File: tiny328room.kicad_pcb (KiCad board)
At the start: 2 copper layers, 105.7 x 23.5 mm, 12 parts, among them K1 PIR, U1 DS18B20, U2 DHT11, U3 TINY328

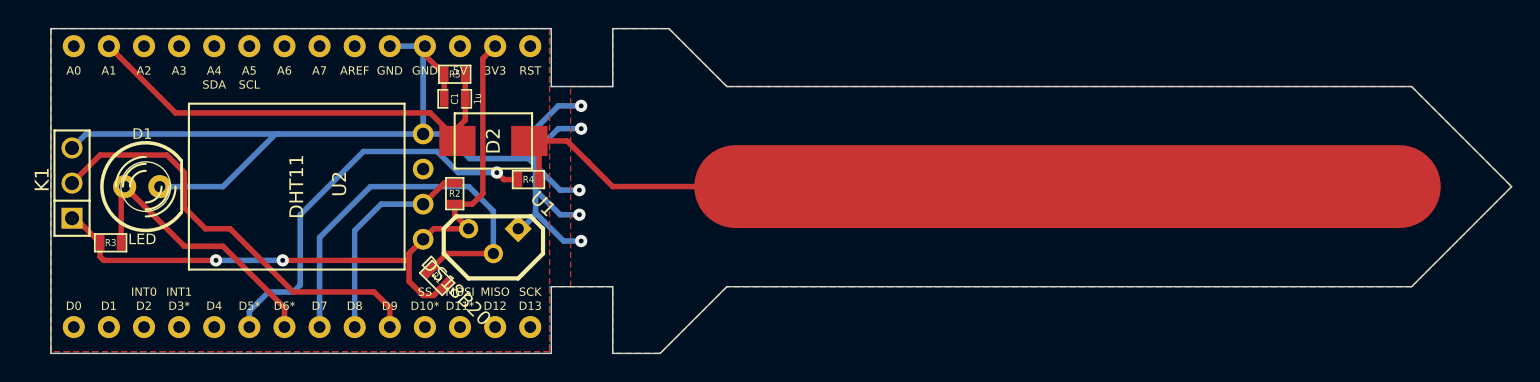
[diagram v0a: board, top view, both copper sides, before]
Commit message: add ambient light sensor
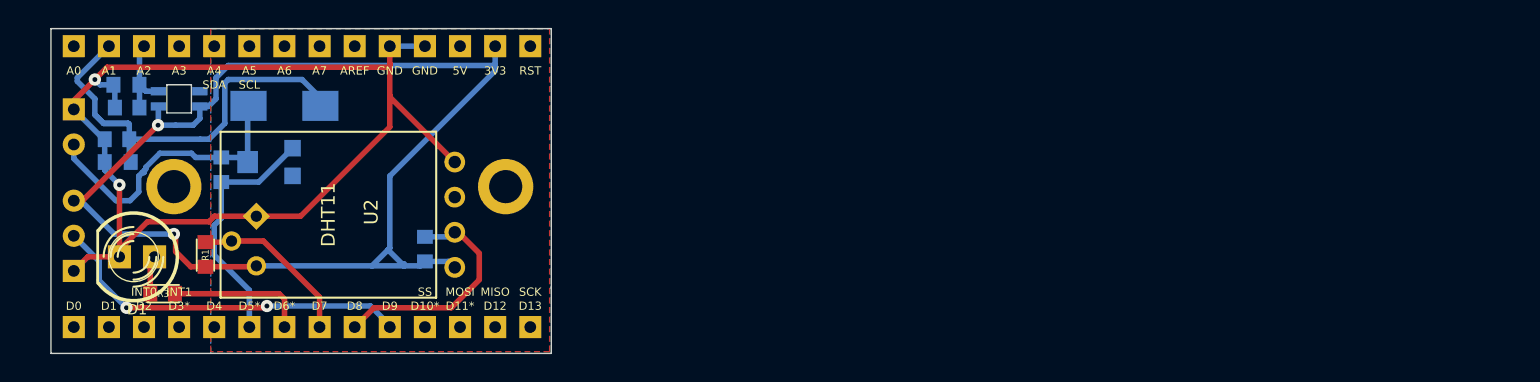
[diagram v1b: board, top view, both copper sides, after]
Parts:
- added 1PIN: P***, 1pin_only, F.Cu at (74.8, 69.8)
- added 1PIN: P***, 1pin_only, F.Cu at (50.8, 69.8)
- added C2: 0.1u, SM0603_C_Hand, B.Cu at (47.4, 62.5)
- added K2: SOIL, PIN_ARRAY_2X1, B.Cu at (43.6, 65.5)
- added R6: 5k, SM0603_Hand, B.Cu at (47.4, 64.1)
- added RV1: 20k, 3305_POT, B.Cu at (57.8, 68.1)
- added U4: APDS-9006-020, APDS-9006-020, B.Cu at (51.2, 63.5)
- C1: footprint SM0603_Capa -> SM0603_C_Hand; moved to B.Cu
- D2, K1, U1: moved to B.Cu
- R1, R3: footprint SM0603 -> SM0603_Hand
- R2, R4, R5: footprint SM0603 -> SM0603_Hand; moved to B.Cu
- moved R5 24.8 mm to (46.7, 66.4)
- moved C1 24.8 mm to (46.7, 68.1)
- moved R4 22.2 mm to (54.2, 68.6), turned to 270 degrees
- moved U1 17.2 mm to (56.8, 73.8), turned to 315 degrees
- moved R1 16.8 mm to (53.1, 74.8), turned to 90 degrees
- moved D2 15.3 mm to (58.8, 64.0), turned to 0 degrees
- moved R3 5.30 mm to (50.0, 77.6), turned to 180 degrees
- moved D1 5.09 mm to (48.1, 74.9), turned to 180 degrees
- moved R2 4.60 mm to (69.0, 74.4)
- moved K1 3.81 mm to (43.6, 73.4), turned to 270 degrees
- moved U2 3.06 mm to (62.0, 71.9)
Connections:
- D1 pad 1: /LED -> N-000004
- R3 pad 1: 3V3 -> /LED
- R3 pad 2: /LED -> N-000004
- U3 pad 17: (no net) -> /BRIGHT
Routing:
- net /CAP_SENSE: track 67.4 -> 21.4 mm
- net 3V3: track 52.2 -> 89.4 mm
- net /DS: track 29.5 -> 12.1 mm
- net N-0000010: track 29.2 -> 17.9 mm, vias 1 -> 0
- net /LED: track 20.8 -> 10.1 mm
- net /BRIGHT: track 0.00 -> 6.14 mm
- net /PIR: track 31.3 -> 26.6 mm, vias 0 -> 2
- net GND: track 86.3 -> 82.8 mm, vias 5 -> 2
- net N-000004: track 0.00 -> 2.79 mm
- net /DHT: track 15.6 -> 17.0 mm
- removed copper zone on F.Cu, net GND
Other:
- board size 105.7 x 23.5 mm -> 36.2 x 23.5 mm
- board text added: "GND"
- board text added: "PIR"
- board text added: "SOIL"
- board text added: "VCC"

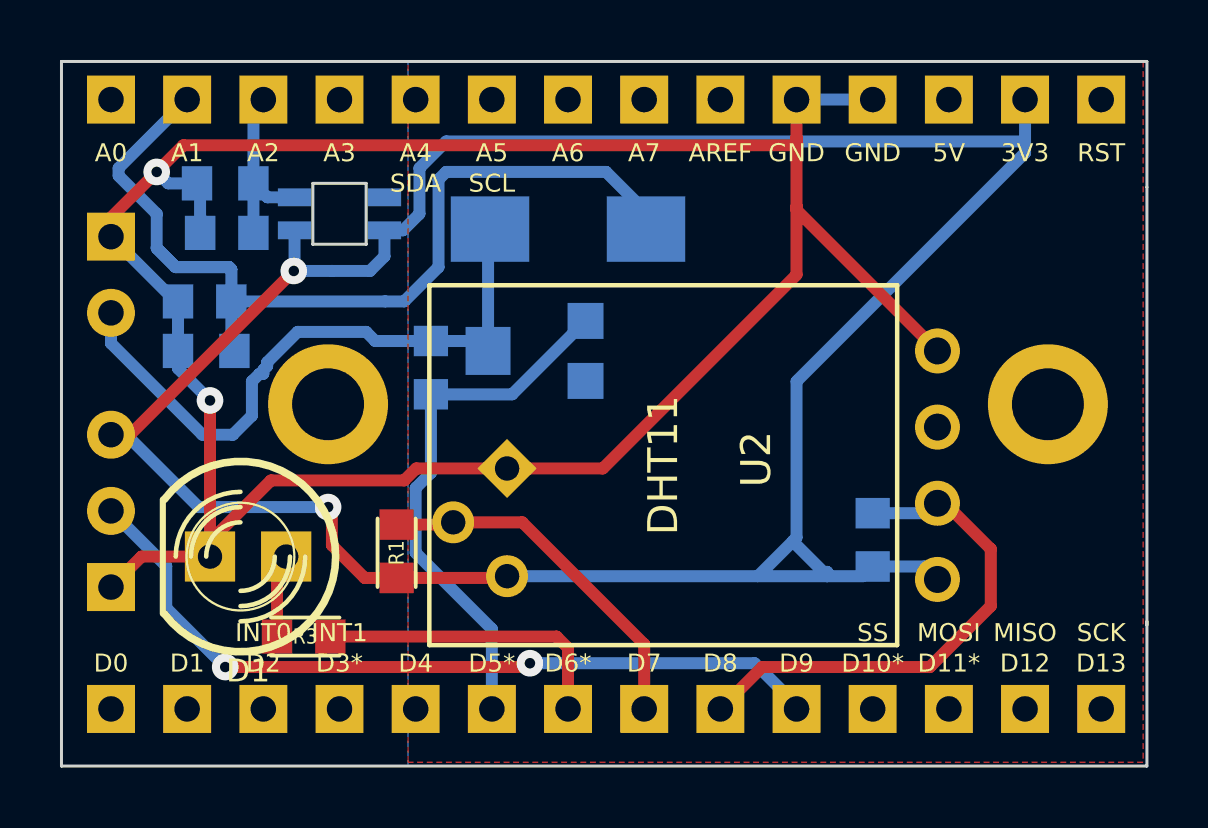
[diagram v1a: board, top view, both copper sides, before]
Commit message: added ultrasonic distance measurer
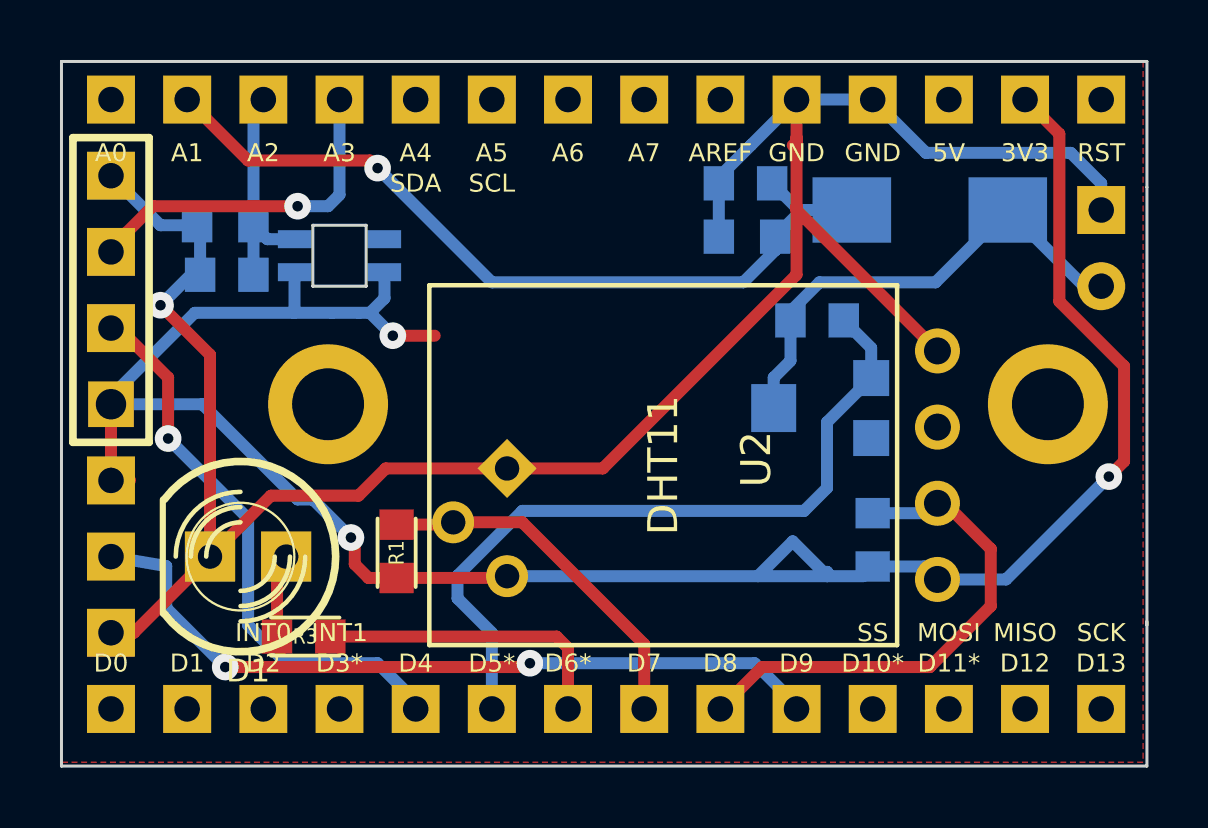
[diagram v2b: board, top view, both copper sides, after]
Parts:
- added K3: DIST, PIN_ARRAY_4x1, F.Cu at (43.6, 66.0)
- moved K2 33.0 mm to (76.6, 64.6)
- moved R5 18.5 mm to (64.8, 62.5)
- moved C1 18.4 mm to (64.8, 64.3)
- moved R4 12.9 mm to (67.1, 67.1), turned to 0 degrees
- moved D2 12.1 mm to (70.9, 63.4), turned to 180 degrees
- moved RV1 9.71 mm to (67.3, 70.0)
- moved K1 1.52 mm to (43.6, 74.9)
- moved U4 1.40 mm to (51.2, 64.9)
- moved C2 1.40 mm to (47.4, 63.9)
- moved R6 1.40 mm to (47.4, 65.5)
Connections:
- net N-0000010 renamed /CAP_TRIG
- net N-000002 renamed /CAP_OUT
- U3 pad 18: (no net) -> /DIST_ECHO
- U3 pad 5: (no net) -> /DIST_TRIG
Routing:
- net /DIST_TRIG: track 0.00 -> 18.8 mm, vias 0 -> 1
- net 3V3: track 89.4 -> 74.2 mm, vias 2 -> 3
- net /DIST_ECHO: track 0.00 -> 11.7 mm, vias 0 -> 1
- net GND: track 82.8 -> 74.9 mm, vias 2 -> 1
- net /CAP_TRIG: track 17.9 -> 25.0 mm
- net /CAP_SENSE: track 21.4 -> 16.7 mm
- net /CAP_OUT: track 33.2 -> 29.0 mm, vias 0 -> 1
- net /BRIGHT: track 6.14 -> 8.01 mm
- net /PIR: track 26.6 -> 25.9 mm
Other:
- outline, holes or cut-outs redrawn
- board text added: "3V3"
- board text added: "CAP SENSE"
- board text added: "DIST_TRIG"
- board text added: "ECHO"
- board text removed: "SOIL"
- board text removed: "VCC"

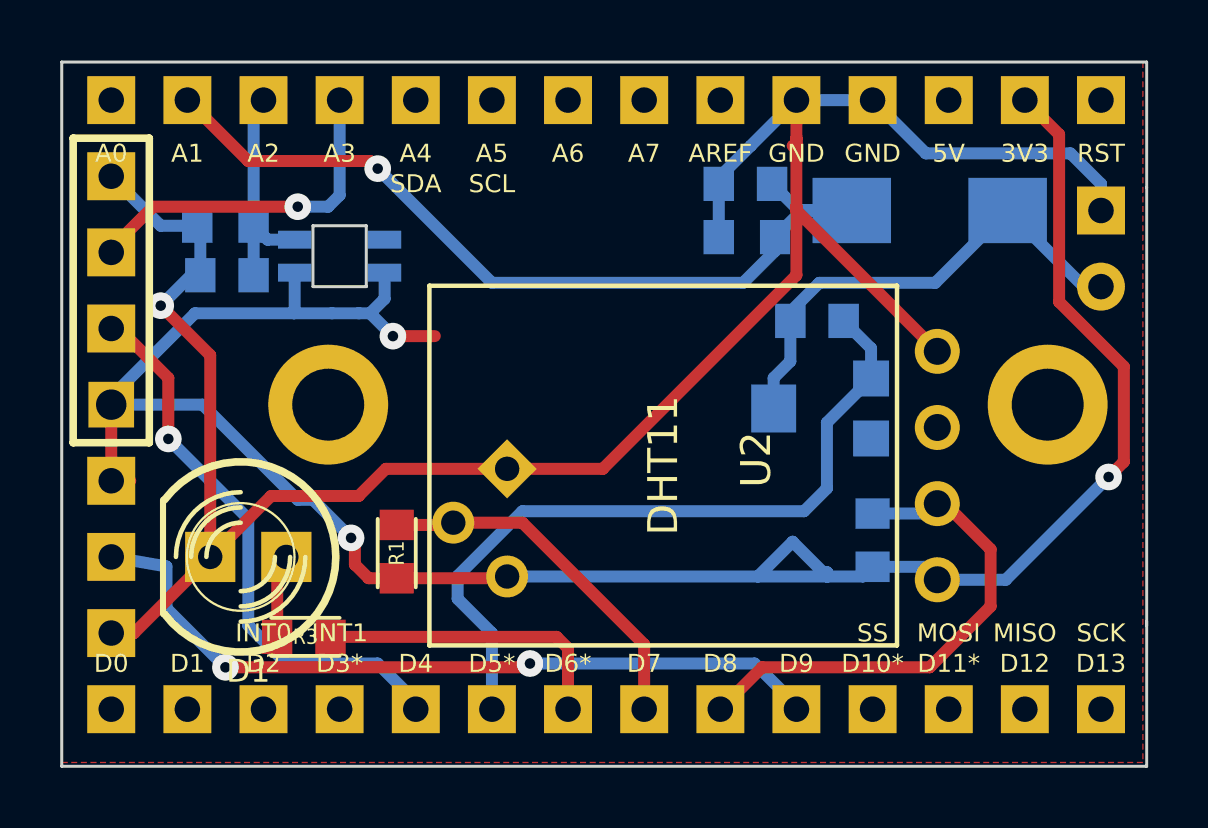
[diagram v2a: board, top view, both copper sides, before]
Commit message: add resistors to FET for stability
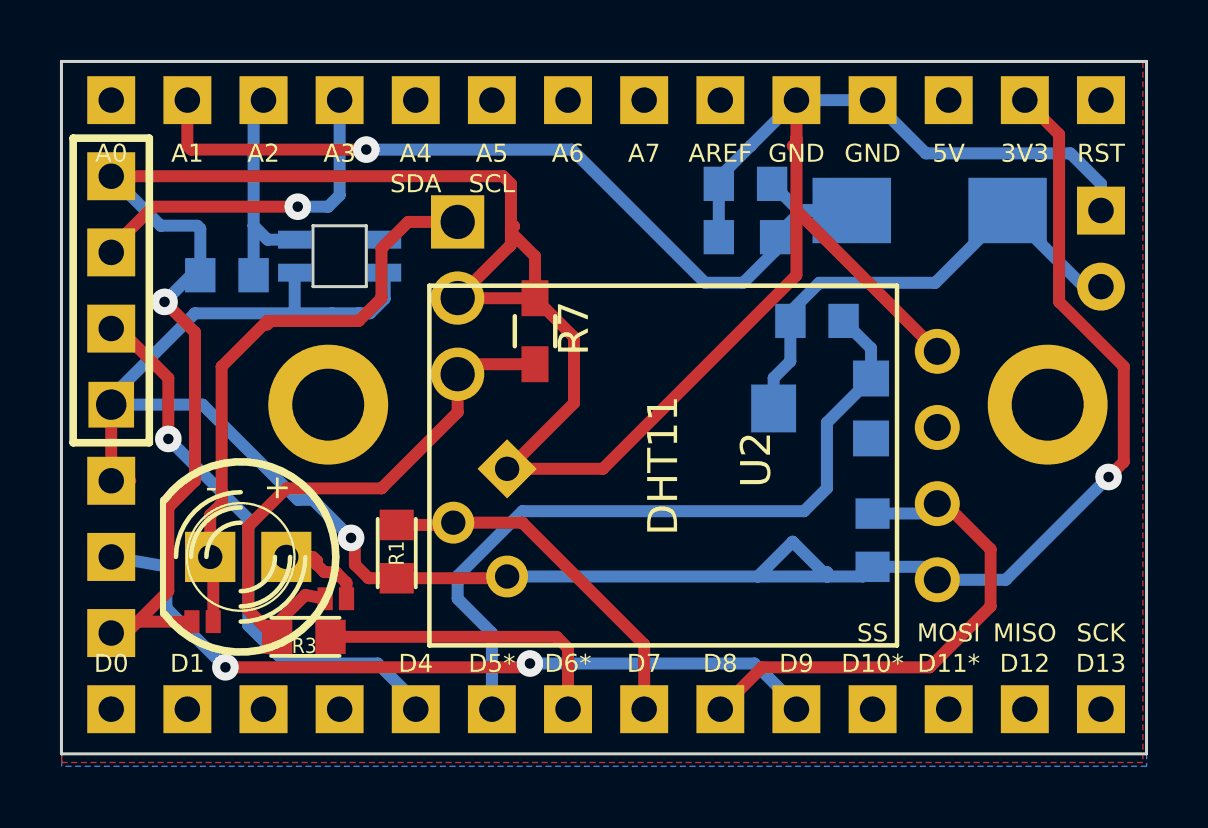
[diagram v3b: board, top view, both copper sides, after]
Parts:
- removed C2: 0.1u, SM0603_C_Hand
- added JP1: LED_DIRECT, S_JUMPER_2, F.Cu at (51.1, 76.3)
- added JP2: LED_DIRECT, S_JUMPER_2, F.Cu at (46.6, 77.1)
- added Q1: IRLZ44N, TO220_MINI2, B.Cu at (55.1, 66.3)
- added R7: 10K, Resistors_SMD:R_0603_HandSoldering, F.Cu at (57.7, 67.4)
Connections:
- D1 pad 1: N-0000033 -> Net-(D1-Pad1)
- D1 pad 2: GND -> Net-(D1-Pad2)
- R3 pad 2: N-0000033 -> Net-(JP1-Pad1)
- RV1 pad 3: (no net) -> Net-(RV1-Pad3)
- U2 pad 3: (no net) -> Net-(U2-Pad3)
- U3 pad 1: (no net) -> Net-(U3-Pad1)
- U3 pad 11: (no net) -> Net-(U3-Pad11)
- U3 pad 12: (no net) -> Net-(U3-Pad12)
- U3 pad 13: (no net) -> Net-(U3-Pad13)
- U3 pad 14: (no net) -> Net-(U3-Pad14)
- U3 pad 15: (no net) -> Net-(U3-Pad15)
- U3 pad 19: (no net) -> Net-(U3-Pad19)
- U3 pad 2: (no net) -> Net-(U3-Pad2)
- U3 pad 20: (no net) -> Net-(U3-Pad20)
- U3 pad 21: (no net) -> Net-(U3-Pad21)
- U3 pad 22: (no net) -> Net-(U3-Pad22)
- U3 pad 23: (no net) -> Net-(U3-Pad23)
- U3 pad 26: (no net) -> +5V
- U3 pad 28: (no net) -> Net-(U3-Pad28)
- U3 pad 3: (no net) -> Net-(U3-Pad3)
- U3 pad 4: (no net) -> Net-(U3-Pad4)
- U4 pad 4: (no net) -> Net-(U4-Pad4)
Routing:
- net GND: track 74.9 -> 96.7 mm
- net Net-(D1-Pad2): track 0.00 -> 19.7 mm
- net Net-(JP1-Pad1): track 0.00 -> 19.1 mm
- net Net-(D1-Pad1): track 0.00 -> 3.15 mm
- net N-0000033: track 2.79 -> 0.00 mm
- net 3V3: track 74.2 -> 71.8 mm, vias 3 -> 2
- net /CAP_OUT: track 29.0 -> 29.9 mm
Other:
- board size 36.2 x 23.5 mm -> 36.2 x 23.1 mm
- board text added: "+"
- board text added: "-"
- board text added: "TRIG"
- board text removed: "DIST_TRIG"
